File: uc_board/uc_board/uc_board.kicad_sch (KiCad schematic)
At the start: 5 parts, among them J1 Conn_01x12

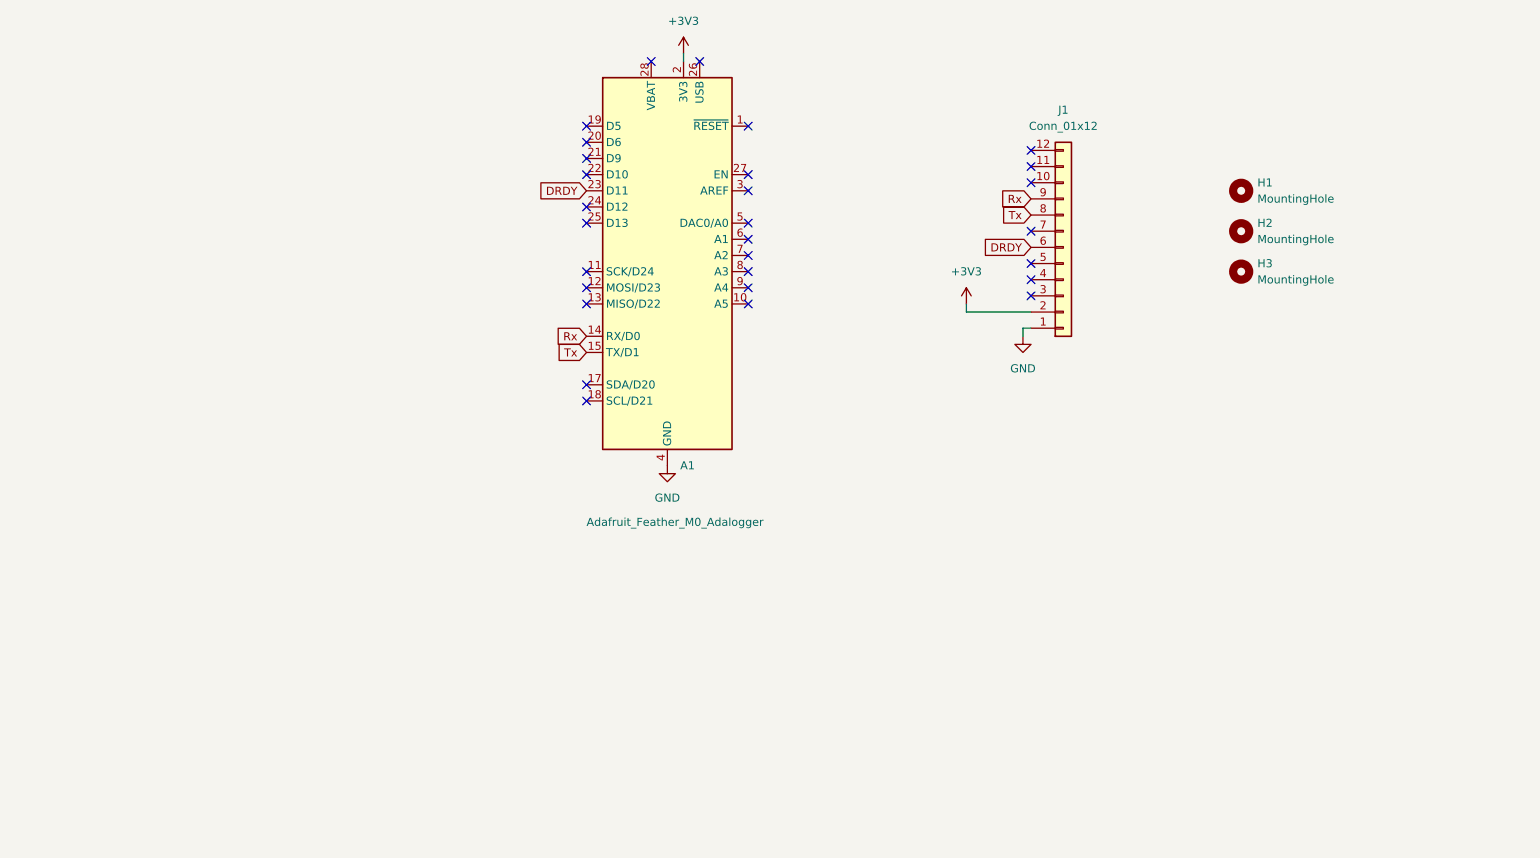
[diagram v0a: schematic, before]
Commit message: Update uc_board and create power card
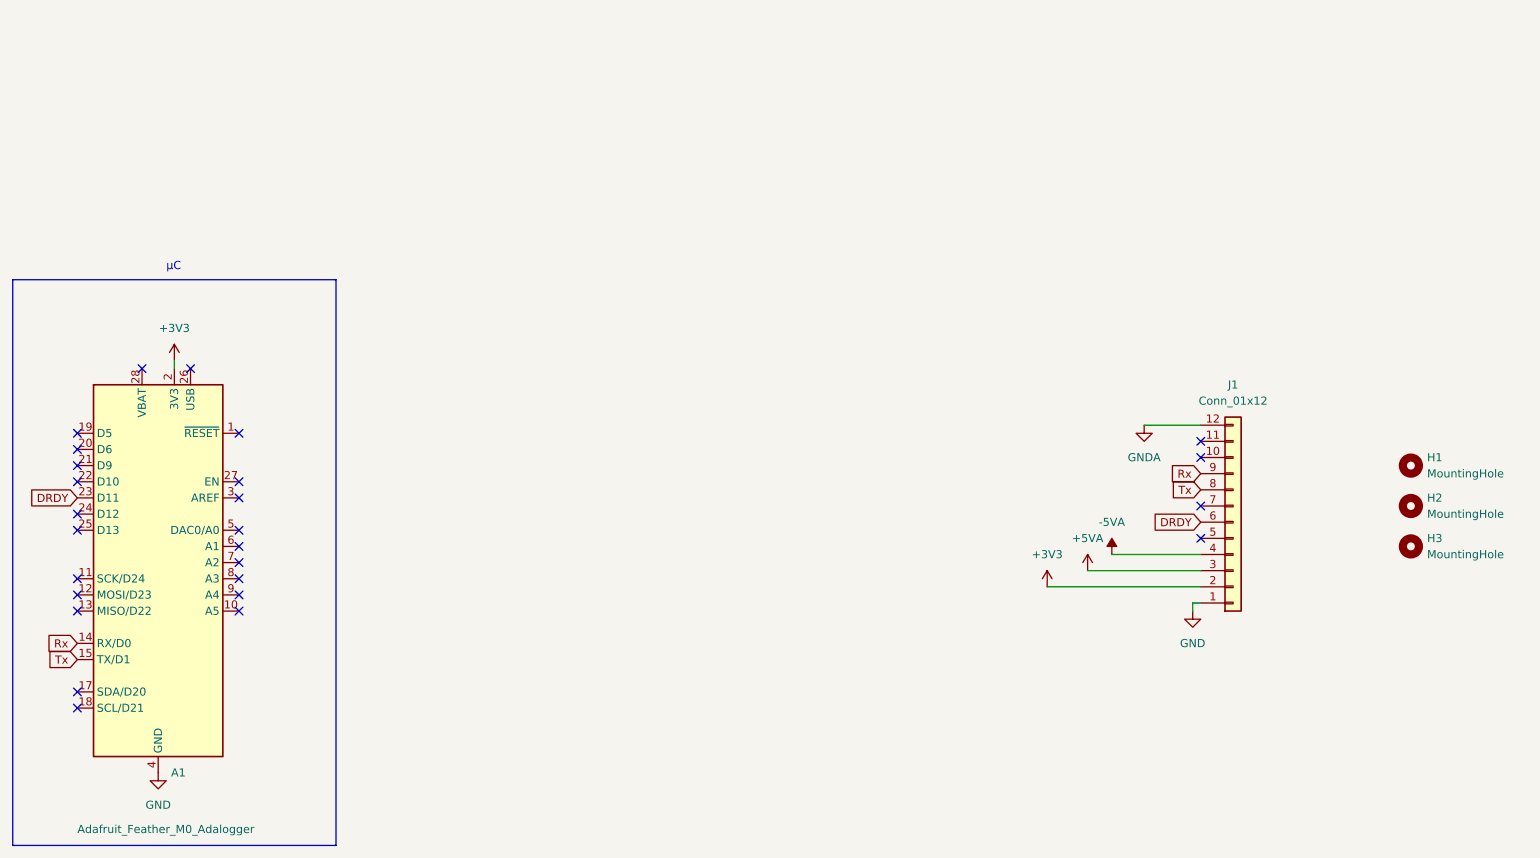
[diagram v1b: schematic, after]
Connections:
- net GNDA: now reaches J1.12 (Pin_12)
- net +5VA: now reaches J1.3 (Pin_3)
- net -5VA: now reaches J1.4 (Pin_4)
- no-connect marks 29 -> 26
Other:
- note added: "µC"
- moved on the sheet: A1, H1, H2, H3, J1

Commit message: update pcb
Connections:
- net Rx: now also J1.8 (Pin_8); no longer J1.9 (Pin_9)
- net Tx: now also J1.9 (Pin_9); no longer J1.8 (Pin_8)
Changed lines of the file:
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@@
     )
   )
-  (global_label "Rx" (shape input) (at 212.09 132.08 180) (fields_autoplaced)
+  (global_label "Rx" (shape input) (at 212.09 134.62 180) (fields_autoplaced)
     (effects (font (size 1.27 1.27)) (justify right))
-    (property "Intersheet References" "${INTERSHEET_REFS}" (id 0) (at 207.3788 132.0006 0)
+    (property "Intersheet References" "${INTERSHEET_REFS}" (id 0) (at 207.3788 134.5406 0)
       (effects (font (size 1.27 1.27)) (justify right) hide)
     )
   )
-  (global_label "Tx" (shape input) (at 212.09 134.62 180) (fields_autoplaced)
+  (global_label "Tx" (shape input) (at 212.09 132.08 180) (fields_autoplaced)
     (effects (font (size 1.27 1.27)) (justify right))
-    (property "Intersheet References" "${INTERSHEET_REFS}" (id 0) (at 207.6812 134.5406 0)
+    (property "Intersheet References" "${INTERSHEET_REFS}" (id 0) (at 207.6812 132.0006 0)
       (effects (font (size 1.27 1.27)) (justify right) hide)
     )
